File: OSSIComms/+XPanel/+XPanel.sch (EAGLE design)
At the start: 19 parts, among them X1 RFCON-MCX-V, X10 P-PAD, X11 P-PAD-S, X2 RFCON-MCX-V, X3 P-PAD-S, X4 P-PAD-S, X5 P-PAD-S, X6 P-PAD, X7 P-PAD, X8 P-PAD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

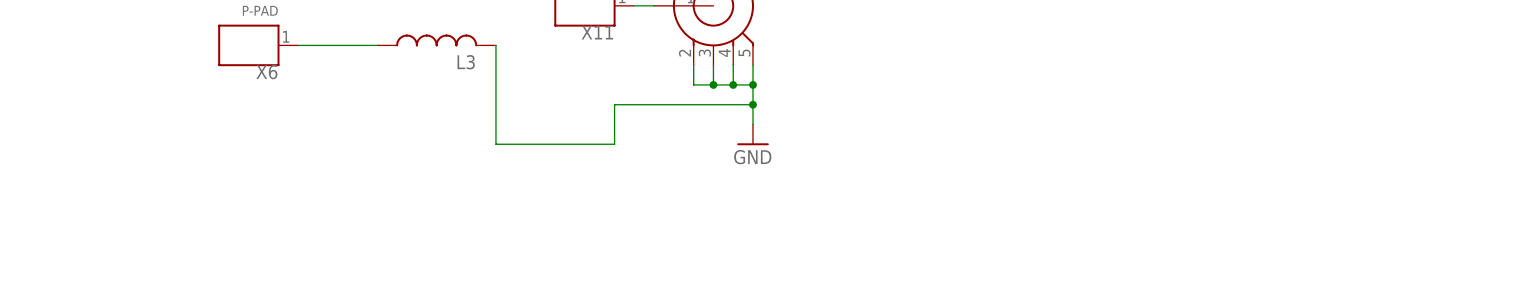
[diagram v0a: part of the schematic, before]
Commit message: new eps board being added
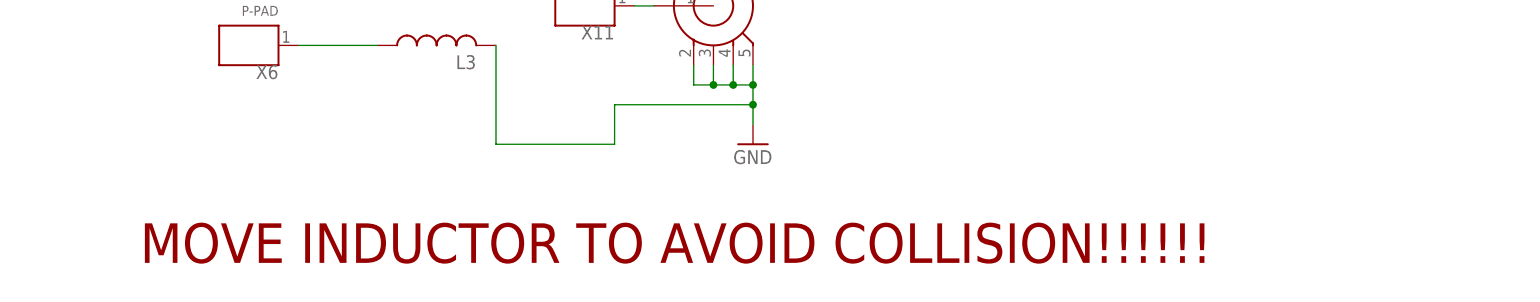
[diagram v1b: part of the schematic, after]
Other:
- note added: "MOVE INDUCTOR TO AVOID COLLISION!!!!!!"
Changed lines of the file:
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@@
 <grid distance="0.1" unitdist="inch" unit="inch" style="lines" multiple="1" display="no" altdistance="0.01" altunitdist="inch" altunit="inch"/>
 <layers>
-<layer number="1" name="Top" color="4" fill="1" visible="yes" active="no"/>
-<layer number="2" name="Route2" color="1" fill="3" visible="yes" active="no"/>
-<layer number="3" name="Route3" color="4" fill="3" visible="yes" active="no"/>
-<layer number="4" name="Route4" color="1" fill="4" visible="yes" active="no"/>
-<layer number="5" name="Route5" color="4" fill="4" visible="yes" active="no"/>
-<layer number="6" name="Route6" color="1" fill="8" visible="yes" active="no"/>
-<layer number="7" name="Route7" color="4" fill="8" visible="yes" active="no"/>
-<layer number="8" name="Route8" color="1" fill="2" visible="yes" active="no"/>
-<layer number="9" name="Route9" color="4" fill="2" visible="yes" active="no"/>
-<layer number="10" name="Route10" color="1" fill="7" visible="yes" active="no"/>
-<layer number="11" name="Route11" color="4" fill="7" visible="yes" active="no"/>
-<layer number="12" name="Route12" color="1" fill="5" visible="yes" active="no"/>
-<layer number="13" name="Route13" color="4" fill="5" visible="yes" active="no"/>
-<layer number="14" name="Route14" color="1" fill="6" visible="yes" active="no"/>
-<layer number="15" name="Route15" color="4" fill="6" visible="yes" active="no"/>
-<layer number="16" name="Bottom" color="1" fill="1" visible="yes" active="no"/>
-<layer number="17" name="Pads" color="2" fill="1" visible="yes" active="no"/>
-<layer number="18" name="Vias" color="2" fill="1" visible="yes" active="no"/>
-<layer number="19" name="Unrouted" color="6" fill="1" visible="yes" active="no"/>
-<layer number="20" name="Dimension" color="15" fill="1" visible="yes" active="no"/>
-<layer number="21" name="tPlace" color="7" fill="1" visible="yes" active="no"/>
-<layer number="22" name="bPlace" color="7" fill="1" visible="yes" active="no"/>
-<layer number="23" name="tOrigins" color="15" fill="1" visible="yes" active="no"/>
-<layer number="24" name="bOrigins" color="15" fill="1" visible="yes" active="no"/>
-<layer number="25" name="tNames" color="7" fill="1" visible="yes" active="no"/>
-<layer number="26" name="bNames" color="7" fill="1" visible="yes" active="no"/>
-<layer number="27" name="tValues" color="7" fill="1" visible="yes" active="no"/>
-<layer number="28" name="bValues" color="7" fill="1" visible="yes" active="no"/>
+<layer number="1" name="Top" color="4" fill="1" visible="no" active="no"/>
+<layer number="2" name="Route2" color="1" fill="3" visible="no" active="no"/>
+<layer number="3" name="Route3" color="4" fill="3" visible="no" active="no"/>
+<layer number="4" name="Route4" color="1" fill="4" visible="no" active="no"/>
+<layer number="5" name="Route5" color="4" fill="4" visible="no" active="no"/>
+<layer number="6" name="Route6" color="1" fill="8" visible="no" active="no"/>
+<layer number="7" name="Route7" color="4" fill="8" visible="no" active="no"/>
+<layer number="8" name="Route8" color="1" fill="2" visible="no" active="no"/>
+<layer number="9" name="Route9" color="4" fill="2" visible="no" active="no"/>
+<layer number="10" name="Route10" color="1" fill="7" visible="no" active="no"/>
+<layer number="11" name="Route11" color="4" fill="7" visible="no" active="no"/>
+<layer number="12" name="Route12" color="1" fill="5" visible="no" active="no"/>
+<layer number="13" name="Route13" color="4" fill="5" visible="no" active="no"/>
+<layer number="14" name="Route14" color="1" fill="6" visible="no" active="no"/>
+<layer number="15" name="Route15" color="4" fill="6" visible="no" active="no"/>
+<layer number="16" name="Bottom" color="1" fill="1" visible="no" active="no"/>
+<layer number="17" name="Pads" color="2" fill="1" visible="no" active="no"/>
+<layer number="18" name="Vias" color="2" fill="1" visible="no" active="no"/>
+<layer number="19" name="Unrouted" color="6" fill="1" visible="no" active="no"/>
+<layer number="20" name="Dimension" color="15" fill="1" visible="no" active="no"/>
+<layer number="21" name="tPlace" color="7" fill="1" visible="no" active="no"/>
+<layer number="22" name="bPlace" color="7" fill="1" visible="no" active="no"/>
+<layer number="23" name="tOrigins" color="15" fill="1" visible="no" active="no"/>
+<layer number="24" name="bOrigins" color="15" fill="1" visible="no" active="no"/>
+<layer number="25" name="tNames" color="7" fill="1" visible="no" active="no"/>
+<layer number="26" name="bNames" color="7" fill="1" visible="no" active="no"/>
+<layer number="27" name="tValues" color="7" fill="1" visible="no" active="no"/>
+<layer number="28" name="bValues" color="7" fill="1" visible="no" active="no"/>
 <layer number="29" name="tStop" color="7" fill="3" visible="no" active="no"/>
 <layer number="30" name="bStop" color="7" fill="6" visible="no" active="no"/>
@@
 <layer number="35" name="tGlue" color="7" fill="4" visible="no" active="no"/>
 <layer number="36" name="bGlue" color="7" fill="5" visible="no" active="no"/>
-<layer number="37" name="tTest" color="7" fill="1" visible="yes" active="no"/>
-<layer number="38" name="bTest" color="7" fill="1" visible="yes" active="no"/>
+<layer number="37" name="tTest" color="7" fill="1" visible="no" active="no"/>
+<layer number="38" name="bTest" color="7" fill="1" visible="no" active="no"/>
 <layer number="39" name="tKeepout" color="4" fill="11" visible="no" active="no"/>
 <layer number="40" name="bKeepout" color="1" fill="11" visible="no" active="no"/>
@@
 <layer number="44" name="Drills" color="7" fill="1" visible="no" active="no"/>
 <layer number="45" name="Holes" color="7" fill="1" visible="no" active="no"/>
-<layer number="46" name="Milling" color="3" fill="1" visible="yes" active="no"/>
-<layer number="47" name="Measures" color="7" fill="1" visible="yes" active="no"/>
-<layer number="48" name="Document" color="7" fill="1" visible="yes" active="no"/>
-<layer number="49" name="Reference" color="7" fill="1" visible="yes" active="no"/>
-<layer number="50" name="dxf" color="7" fill="1" visible="yes" active="no"/>
-<layer number="51" name="tDocu" color="14" fill="1" visible="yes" active="no"/>
-<layer number="52" name="bDocu" color="7" fill="1" visible="yes" active="no"/>
-<layer number="53" name="tGND_GNDA" color="7" fill="9" visible="yes" active="no"/>
-<layer number="54" name="bGND_GNDA" color="1" fill="9" visible="yes" active="no"/>
-<layer number="56" name="wert" color="7" fill="1" visible="yes" active="no"/>
+<layer number="46" name="Milling" color="3" fill="1" visible="no" active="no"/>
+<layer number="47" name="Measures" color="7" fill="1" visible="no" active="no"/>
+<layer number="48" name="Document" color="7" fill="1" visible="no" active="no"/>
+<layer number="49" name="Reference" color="7" fill="1" visible="no" active="no"/>
+<layer number="50" name="dxf" color="7" fill="1" visible="no" active="no"/>
+<layer number="51" name="tDocu" color="14" fill="1" visible="no" active="no"/>
+<layer number="52" name="bDocu" color="7" fill="1" visible="no" active="no"/>
+<layer number="53" name="tGND_GNDA" color="7" fill="9" visible="no" active="no"/>
+<layer number="54" name="bGND_GNDA" color="1" fill="9" visible="no" active="no"/>
+<layer number="56" name="wert" color="7" fill="1" visible="no" active="no"/>
 <layer number="91" name="Nets" color="2" fill="1" visible="yes" active="yes"/>
 <layer number="92" name="Busses" color="1" fill="1" visible="yes" active="yes"/>
@@
 <plain>
 <text x="172.72" y="114.3" size="1.778" layer="94">LC Balun</text>
+<text x="121.92" y="58.42" size="5.08" layer="94">MOVE INDUCTOR TO AVOID COLLISION!!!!!!</text>
 </plain>
 <instances>
